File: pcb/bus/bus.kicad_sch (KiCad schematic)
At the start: 7 parts, among them U101 USBLC6-2SC6, U102 FE1.1s, Y101 12MHz

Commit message: update bus pcb
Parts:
- added H101, H102, H103, H104: MountingHole_Pad, MountingHole:MountingHole_3.2mm_M3_Pad_Via, symbol Mechanical:MountingHole_Pad
- added R102, R103, R104, R105: R/C/0Ohm, Resistor_SMD:R_0805_2012Metric, symbol Device:R
- Y101: footprint Embedded_Lib:M49S-SMD -> PRJ:M49S-SMD
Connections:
- net GND: now also R102.1, R103.1, R104.1, R105.1
- new net: H102.1, R103.2
- new net: H103.1, R104.2
- new net: H104.1, R105.2
- new net: H101.1, R102.2
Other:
- sheet RPI renamed RPI Connector
- added sheet Device Connector 1 (device_connector.kicad_sch)
- added sheet Device Connector 2 (device_connector.kicad_sch)
- added sheet Device Connector 3 (device_connector.kicad_sch)
- added sheet Device Connector 4 (device_connector.kicad_sch)
- added sheet Power Connector (power_connector.kicad_sch)
- sheet RPI Connector ports: added I2C_SCL, I2C_SDA; removed none

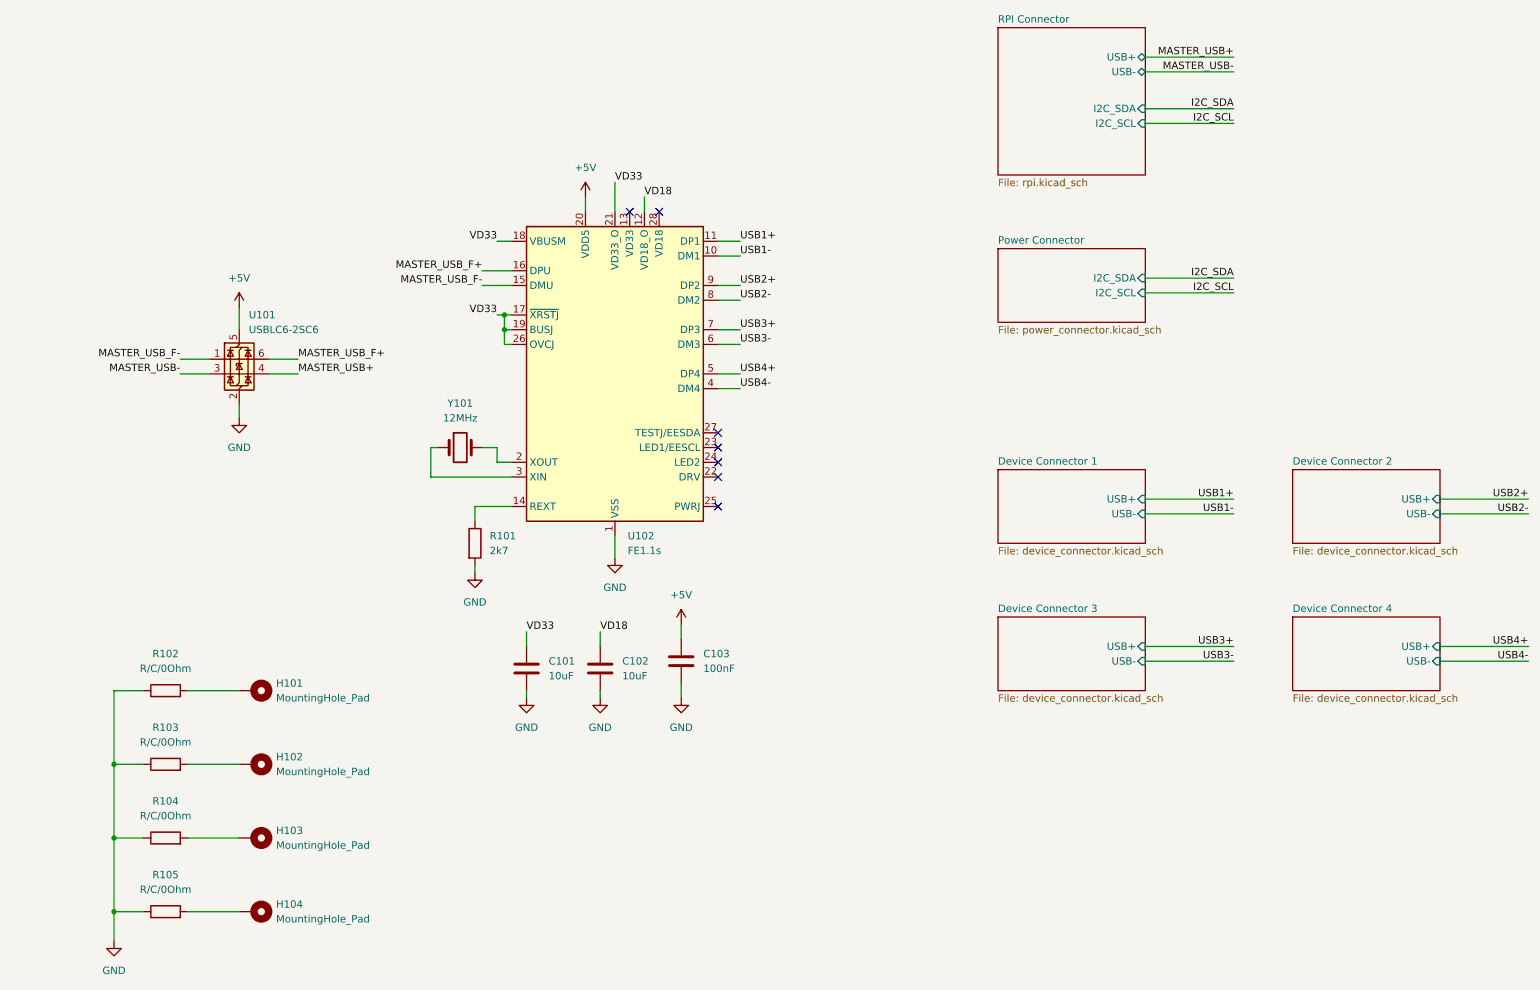
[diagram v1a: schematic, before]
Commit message: update pcb size
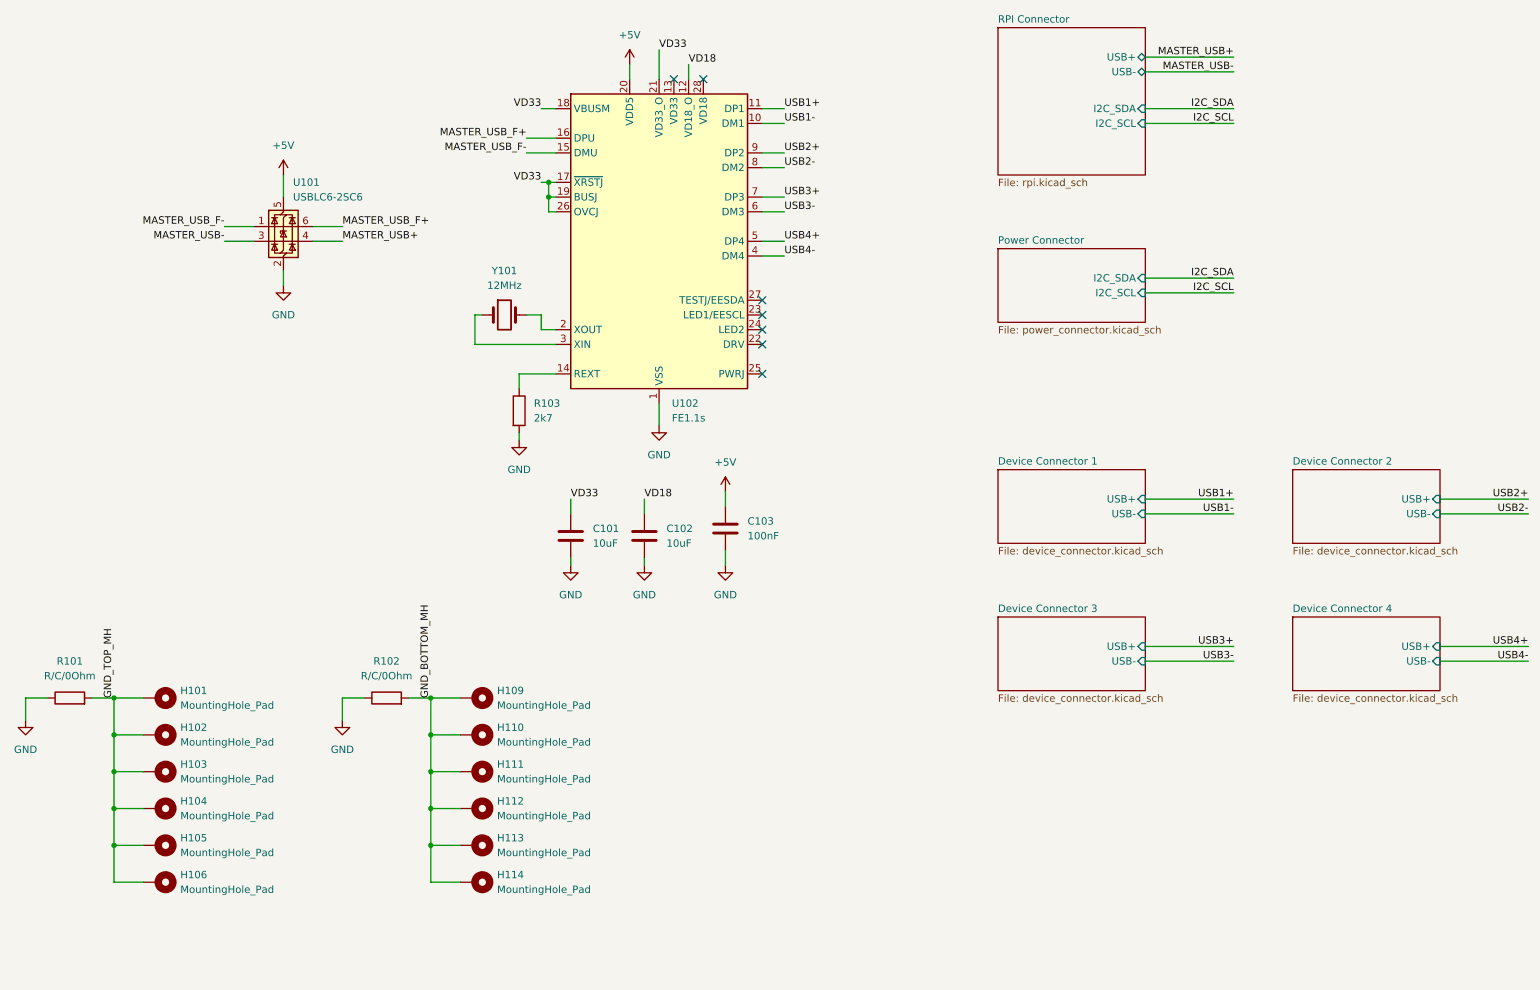
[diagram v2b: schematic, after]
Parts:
- removed R103, R104, R105: R/C/0Ohm, Resistor_SMD:R_0805_2012Metric, symbol Device:R
- added H105, H106, H109, H110, H111, H112, H113, H114: MountingHole_Pad, MountingHole:MountingHole_2.7mm_M2.5_Pad_TopBottom, symbol Mechanical:MountingHole_Pad
- added R102: R/C/0Ohm, Resistor_SMD:R_0805_2012Metric, symbol Device:R
- H101, H102, H103, H104: footprint MountingHole:MountingHole_3.2mm_M3_Pad_Via -> MountingHole:MountingHole_2.7mm_M2.5_Pad_TopBottom
- renumbered R102 to R101, R101 to R103
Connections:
- net GND: now also R102.1
- net GND_TOP_MH: now reaches H102.1
- net GND_TOP_MH: now also H101.1, H103.1, H104.1, R101.2, H105.1, H106.1
- new net GND_BOTTOM_MH: H109.1, H110.1, H111.1, H112.1, H113.1, H114.1, R102.2
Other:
- moved on the sheet: C101, C102, C103, H101, H102, R101, R103, U101, U102, Y101

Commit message: update bus pcb
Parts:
- removed U101: USBLC6-2SC6, Package_TO_SOT_SMD:SOT-666, symbol Power_Protection:USBLC6-2SC6
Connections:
- net MASTER_USB_F+ is gone; now on net MASTER_USB+: U102.16 (DPU)
- net MASTER_USB_F- is gone; now on net MASTER_USB-: U102.15 (DMU)

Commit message: update hole size
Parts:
- H101, H102, H103, H104, H105, H106, H109, H110, H111, H112, H113, H114: footprint MountingHole:MountingHole_2.7mm_M2.5_Pad_TopBottom -> MountingHole:MountingHole_3.2mm_M3_Pad_TopBottom
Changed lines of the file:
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@@
 			)
 		)
-		(property "Footprint" "MountingHole:MountingHole_2.7mm_M2.5_Pad_TopBottom"
+		(property "Footprint" "MountingHole:MountingHole_3.2mm_M3_Pad_TopBottom"
 			(at 100.33 153.67 0)
 			(effects
@@
 			)
 		)
-		(property "Footprint" "MountingHole:MountingHole_2.7mm_M2.5_Pad_TopBottom"
+		(property "Footprint" "MountingHole:MountingHole_3.2mm_M3_Pad_TopBottom"
 			(at 100.33 160.02 0)
 			(effects
@@
 			)
 		)
-		(property "Footprint" "MountingHole:MountingHole_2.7mm_M2.5_Pad_TopBottom"
+		(property "Footprint" "MountingHole:MountingHole_3.2mm_M3_Pad_TopBottom"
 			(at 45.72 166.37 0)
 			(effects
@@
 			)
 		)
-		(property "Footprint" "MountingHole:MountingHole_2.7mm_M2.5_Pad_TopBottom"
+		(property "Footprint" "MountingHole:MountingHole_3.2mm_M3_Pad_TopBottom"
 			(at 45.72 160.02 0)
 			(effects
@@
 			)
 		)
-		(property "Footprint" "MountingHole:MountingHole_2.7mm_M2.5_Pad_TopBottom"
+		(property "Footprint" "MountingHole:MountingHole_3.2mm_M3_Pad_TopBottom"
 			(at 100.33 166.37 0)
 			(effects
@@
 			)
 		)
-		(property "Footprint" "MountingHole:MountingHole_2.7mm_M2.5_Pad_TopBottom"
+		(property "Footprint" "MountingHole:MountingHole_3.2mm_M3_Pad_TopBottom"
 			(at 45.72 147.32 0)
 			(effects
@@
 			)
 		)
-		(property "Footprint" "MountingHole:MountingHole_2.7mm_M2.5_Pad_TopBottom"
+		(property "Footprint" "MountingHole:MountingHole_3.2mm_M3_Pad_TopBottom"
 			(at 45.72 140.97 0)
 			(effects
@@
 			)
 		)
-		(property "Footprint" "MountingHole:MountingHole_2.7mm_M2.5_Pad_TopBottom"
+		(property "Footprint" "MountingHole:MountingHole_3.2mm_M3_Pad_TopBottom"
 			(at 100.33 172.72 0)
 			(effects
@@
 			)
 		)
-		(property "Footprint" "MountingHole:MountingHole_2.7mm_M2.5_Pad_TopBottom"
+		(property "Footprint" "MountingHole:MountingHole_3.2mm_M3_Pad_TopBottom"
 			(at 45.72 172.72 0)
 			(effects
@@
 			)
 		)
-		(property "Footprint" "MountingHole:MountingHole_2.7mm_M2.5_Pad_TopBottom"
+		(property "Footprint" "MountingHole:MountingHole_3.2mm_M3_Pad_TopBottom"
 			(at 45.72 153.67 0)
 			(effects
@@
 			)
 		)
-		(property "Footprint" "MountingHole:MountingHole_2.7mm_M2.5_Pad_TopBottom"
+		(property "Footprint" "MountingHole:MountingHole_3.2mm_M3_Pad_TopBottom"
 			(at 100.33 147.32 0)
 			(effects
@@
 			)
 		)
-		(property "Footprint" "MountingHole:MountingHole_2.7mm_M2.5_Pad_TopBottom"
+		(property "Footprint" "MountingHole:MountingHole_3.2mm_M3_Pad_TopBottom"
 			(at 100.33 140.97 0)
 			(effects

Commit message: fixes
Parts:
- removed H101, H102, H103, H104, H105, H106, H109, H110, H111, H112, H113, H114: MountingHole_Pad, MountingHole:MountingHole_3.2mm_M3_Pad_TopBottom, symbol Mechanical:MountingHole_Pad
- removed R101, R102: R/C/0Ohm, Resistor_SMD:R_0805_2012Metric, symbol Device:R
- added H101, H102, H103, H104, H105, H106, H107, H108, H109, H110, H111, H112: MountingHole, MountingHole:MountingHole_3.2mm_M3, symbol Mechanical:MountingHole

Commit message: update ALL parts
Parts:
- C101, C102: LCSC C307560 -> C13585
- C103: LCSC C354365 -> C28233
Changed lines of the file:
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@@
+			)
+		)
+		(property "MOUSER" ""
+			(at 132.08 62.23 0)
+			(effects
+				(font
+					(size 1.27 1.27)
+				)
 			)
 		)
@@
 			)
 		)
-		(property "LCSC" "C307560"
+		(property "LCSC" "C13585"
 			(at 116.84 113.03 0)
 			(effects
@@
 				)
 				(hide yes)
+			)
+		)
+		(property "MOUSER" ""
+			(at 116.84 113.03 0)
+			(effects
+				(font
+					(size 1.27 1.27)
+				)
 			)
 		)
@@
 			)
 		)
+		(property "MOUSER" ""
+			(at 38.1 146.05 0)
+			(effects
+				(font
+					(size 1.27 1.27)
+				)
+			)
+		)
 		(instances
 			(project "bus"
@@
 			)
 		)
-		(property "LCSC" "C354365"
+		(property "LCSC" "C28233"
 			(at 143.51 111.76 0)
 			(effects
@@
 				)
 				(hide yes)
+			)
+		)
+		(property "MOUSER" ""
+			(at 143.51 111.76 0)
+			(effects
+				(font
+					(size 1.27 1.27)
+				)
 			)
 		)
@@
 			)
 		)
+		(property "MOUSER" ""
+			(at 38.1 165.1 0)
+			(effects
+				(font
+					(size 1.27 1.27)
+				)
+			)
+		)
 		(instances
 			(project "bus"
@@
 			)
 		)
+		(property "MOUSER" ""
+			(at 63.5 146.05 0)
+			(effects
+				(font
+					(size 1.27 1.27)
+				)
+			)
+		)
 		(instances
 			(project "bus"
@@
 			)
 		)
+		(property "MOUSER" ""
+			(at 38.1 139.7 0)
+			(effects
+				(font
+					(size 1.27 1.27)
+				)
+			)
+		)
 		(instances
 			(project ""
@@
 			)
 		)
+		(property "MOUSER" ""
+			(at 38.1 171.45 0)
+			(effects
+				(font
+					(size 1.27 1.27)
+				)
+			)
+		)
 		(instances
 			(project "bus"
@@
 			)
 		)
+		(property "MOUSER" ""
+			(at 38.1 158.75 0)
+			(effects
+				(font
+					(size 1.27 1.27)
+				)
+			)
+		)
 		(instances
 			(project "bus"
@@
 				)
 				(hide yes)
+			)
+		)
+		(property "MOUSER" ""
+			(at 105.41 74.93 0)
+			(effects
+				(font
+					(size 1.27 1.27)
+				)
 			)
 		)
@@
 			)
 		)
+		(property "MOUSER" ""
+			(at 63.5 158.75 0)
+			(effects
+				(font
+					(size 1.27 1.27)
+				)
+			)
+		)
 		(instances
 			(project "bus"
@@
 			)
 		)
+		(property "MOUSER" ""
+			(at 63.5 139.7 0)
+			(effects
+				(font
+					(size 1.27 1.27)
+				)
+			)
+		)
 		(instances
 			(project "bus"
@@
 			)
 		)
+		(property "MOUSER" ""
+			(at 63.5 152.4 0)
+			(effects
+				(font
+					(size 1.27 1.27)
+				)
+			)
+		)
 		(instances
 			(project "bus"
@@
 			)
 		)
-		(property "LCSC" "C307560"
+		(property "LCSC" "C13585"
 			(at 129.54 113.03 0)
 			(effects
@@
 				)
 				(hide yes)
+			)
+		)
+		(property "MOUSER" ""
+			(at 129.54 113.03 0)
+			(effects
+				(font
+					(size 1.27 1.27)
+				)
 			)
 		)
@@
 			)
 		)
+		(property "MOUSER" ""
+			(at 38.1 152.4 0)
+			(effects
+				(font
+					(size 1.27 1.27)
+				)
+			)
+		)
 		(instances
 			(project "bus"
@@
 			)
 		)
+		(property "MOUSER" ""
+			(at 63.5 165.1 0)
+			(effects
+				(font
+					(size 1.27 1.27)
+				)
+			)
+		)
 		(instances
 			(project "bus"
@@
 				)
 				(hide yes)
+			)
+		)
+		(property "MOUSER" ""
+			(at 107.95 91.44 0)
+			(effects
+				(font
+					(size 1.27 1.27)
+				)
 			)
 		)
@@
 			)
 		)
+		(property "MOUSER" ""
+			(at 63.5 171.45 0)
+			(effects
+				(font
+					(size 1.27 1.27)
+				)
+			)
+		)

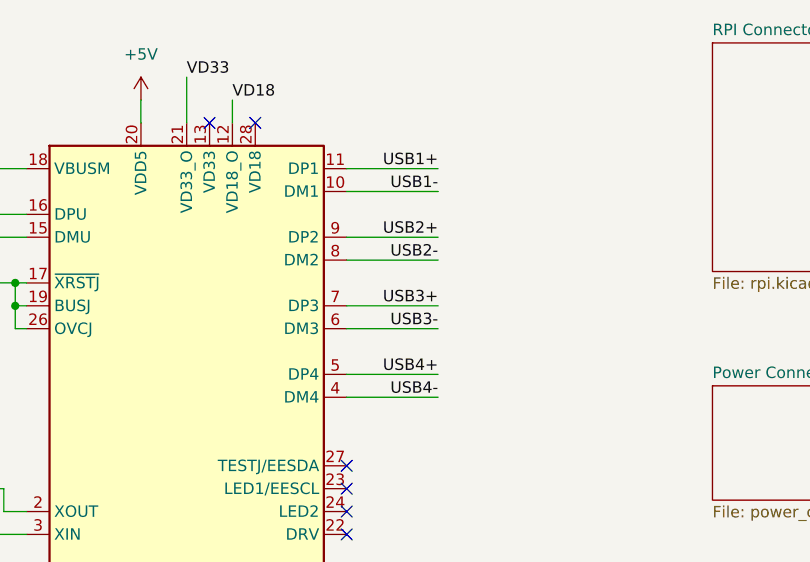
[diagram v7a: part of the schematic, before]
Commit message: move smd parts to backside - no usb length improvements
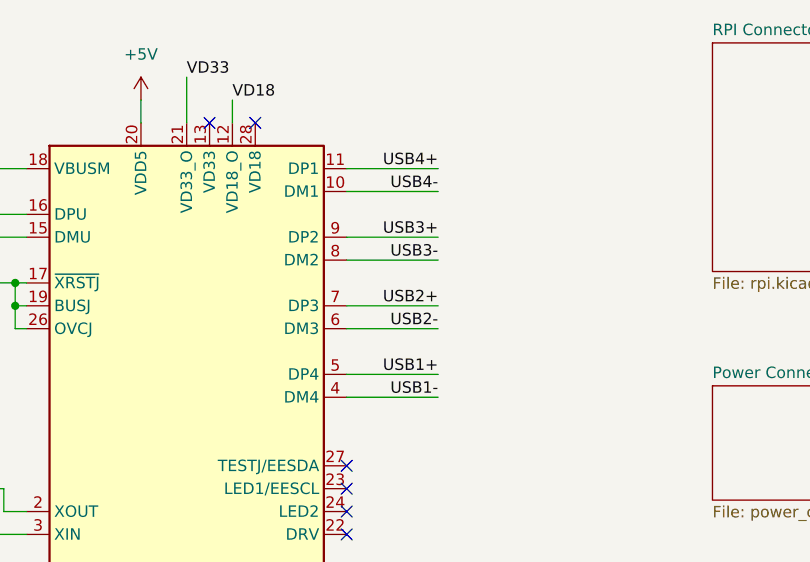
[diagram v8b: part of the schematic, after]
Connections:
- net USB1+: now also U102.5 (DP4); no longer U102.11 (DP1)
- net USB1-: now also U102.4 (DM4); no longer U102.10 (DM1)
- net USB2+: now also U102.7 (DP3); no longer U102.9 (DP2)
- net USB2-: now also U102.6 (DM3); no longer U102.8 (DM2)
- net USB3+: now also U102.9 (DP2); no longer U102.7 (DP3)
- net USB3-: now also U102.8 (DM2); no longer U102.6 (DM3)
- net USB4+: now also U102.11 (DP1); no longer U102.5 (DP4)
- net USB4-: now also U102.10 (DM1); no longer U102.4 (DM4)
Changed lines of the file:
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@@
 		)
 	)
-	(label "USB1+"
+	(label "USB4+"
 		(at 160.02 39.37 180)
 		(effects
@@
 		)
 	)
-	(label "USB4-"
+	(label "USB1-"
 		(at 160.02 64.77 180)
 		(effects
@@
 		)
 	)
-	(label "USB3-"
+	(label "USB2-"
 		(at 160.02 57.15 180)
 		(effects
@@
 		)
 	)
-	(label "USB1-"
+	(label "USB4-"
 		(at 160.02 41.91 180)
 		(effects
@@
 		)
 	)
-	(label "USB3+"
+	(label "USB2+"
 		(at 160.02 54.61 180)
 		(effects
@@
 		)
 	)
-	(label "USB2+"
+	(label "USB3+"
 		(at 160.02 46.99 180)
 		(effects
@@
 		)
 	)
-	(label "USB4+"
+	(label "USB1+"
 		(at 160.02 62.23 180)
 		(effects
@@
 		)
 	)
-	(label "USB2-"
+	(label "USB3-"
 		(at 160.02 49.53 180)
 		(effects
